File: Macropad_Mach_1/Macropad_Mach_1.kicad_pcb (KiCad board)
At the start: 2 copper layers, 88.4 x 102.5 mm, 39 parts, among them J1 Conn_01x12, J2 Conn_01x12, SW1 RotaryEncoder_Switch_MP

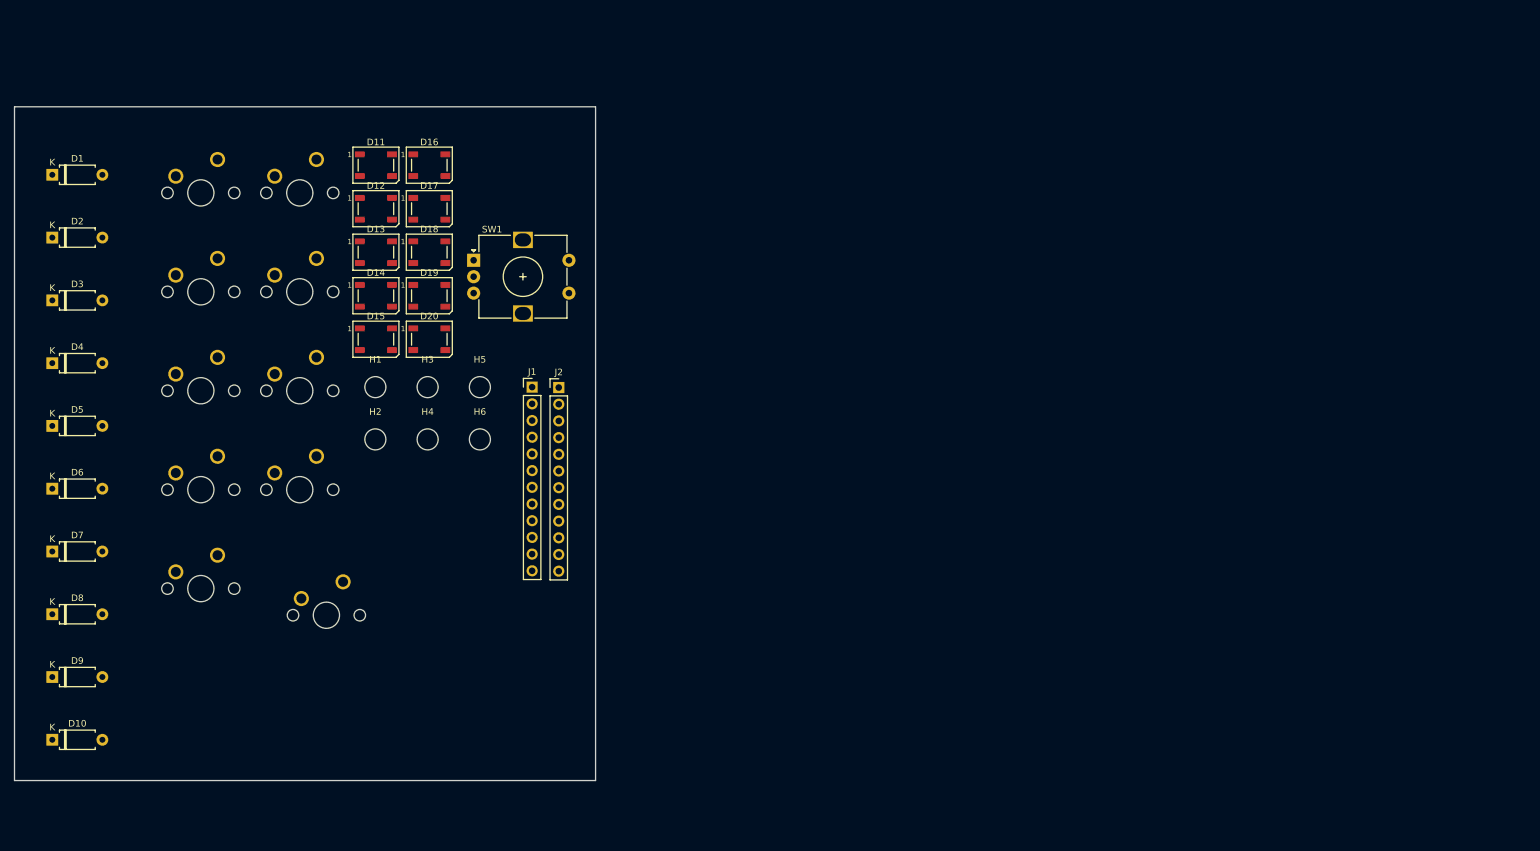
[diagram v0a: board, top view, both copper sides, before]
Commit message: feat: update PCB with APA102-2020 LEDs, keyboard layout, and encoder
- Replaced LEDs with APA102-2020
- Created the keyboard layout
- Added Edgecuts
- Routed the keys
- Integrated the encoder into the layout
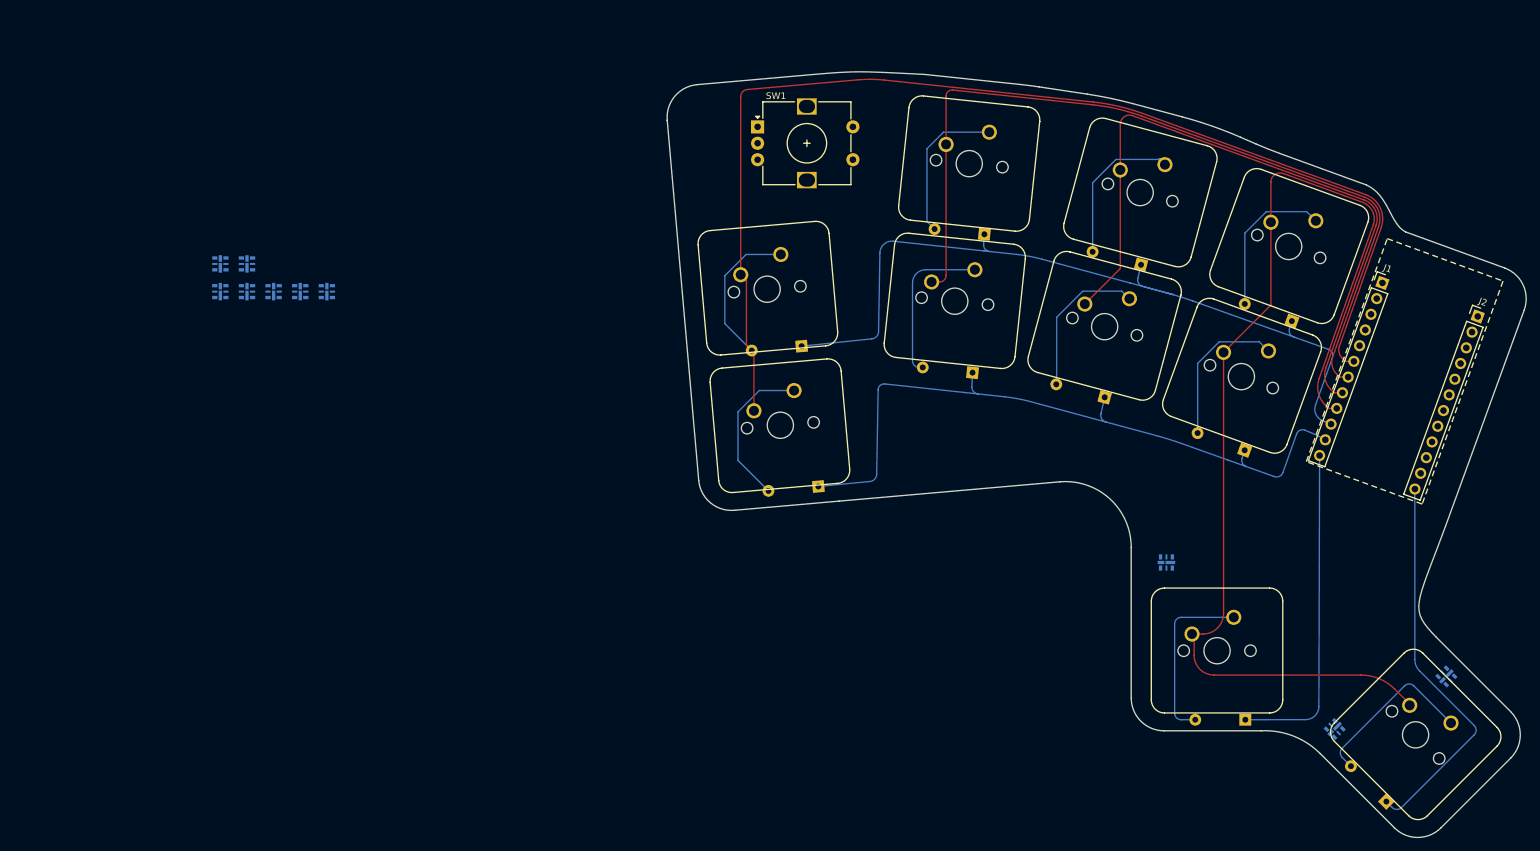
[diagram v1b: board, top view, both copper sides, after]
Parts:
- removed D11, D12, D13, D14, D15, D16, D17, D18, D19, D20: WS2812B, LED_SMD:LED_WS2812B_PLCC4_5.0x5.0mm_P3.2mm
- removed H1, H2, H3, H4, H5, H6: MountingHole, MountingHole:MountingHole_3.2mm_M3
- added D21: APA102-2020, LED_SMD:LED-APA102-2020, B.Cu at (267.6, 133.4)
- added D22: APA102-2020, LED_SMD:LED-APA102-2020, B.Cu at (250.6, 141.4)
- added D23: APA102-2020, LED_SMD:LED-APA102-2020, B.Cu at (225.0, 116.1)
- added D24: APA102-2020, LED_SMD:LED-APA102-2020, B.Cu at (85.1, 70.7)
- added D25: APA102-2020, LED_SMD:LED-APA102-2020, B.Cu at (81.1, 70.7)
- added D26: APA102-2020, LED_SMD:LED-APA102-2020, B.Cu at (97.3, 74.9)
- added D27: APA102-2020, LED_SMD:LED-APA102-2020, B.Cu at (93.2, 74.9)
- added D28: APA102-2020, LED_SMD:LED-APA102-2020, B.Cu at (89.2, 74.9)
- added D29: APA102-2020, LED_SMD:LED-APA102-2020, B.Cu at (85.1, 74.9)
- added D30: APA102-2020, LED_SMD:LED-APA102-2020, B.Cu at (81.1, 74.9)
- D1, D10, D2, D3, D4, D5, D6, D7, D8, D9: moved to B.Cu
- moved D10 203.2 mm to (258.4, 152.4), turned to 135 degrees
- moved D4 188.7 mm to (244.1, 79.4), turned to 160 degrees
- moved D8 183.1 mm to (236.9, 99.0), turned to 160 degrees
- moved D9 181.6 mm to (237.0, 140.0), turned to 180 degrees
- moved MX4 169.6 mm to (243.6, 68.0), turned to -20 degrees
- moved MX10 166.7 mm to (262.9, 142.3), turned to -45 degrees
- moved D3 165.7 mm to (221.1, 70.8), turned to 165 degrees
- moved D7 161.8 mm to (215.6, 91.0), turned to 165 degrees
- moved MX3 146.0 mm to (221.0, 59.8), turned to -15 degrees
- moved MX8 143.3 mm to (236.4, 87.8), turned to -20 degrees
- moved D2 141.8 mm to (197.3, 66.2), turned to 174 degrees
- moved MX9 141.7 mm to (232.7, 129.5)
- moved D6 141.1 mm to (195.5, 87.2), turned to 174 degrees
- moved J2 140.2 mm to (272.4, 78.6), turned to -20 degrees
- moved J1 130.3 mm to (257.9, 73.5), turned to -20 degrees
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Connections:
- J1 pad 10: Row_0 -> Col_3
- J1 pad 11: Row_1 -> Row_0
- J1 pad 12: Row_2 -> Row_1
- J1 pad 5: unconnected-(J1-Pin_5-Pad5) -> SDA
- J1 pad 6: Col_0 -> SCL
- J1 pad 7: Col_1 -> Col_0
- J1 pad 8: Col_2 -> Col_1
- J1 pad 9: Col_3 -> Col_2
- J2 pad 11: unconnected-(J2-Pin_11-Pad11) -> Row_3
- J2 pad 12: Row_3 -> Row_2
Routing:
- net Col_0: track 0.00 -> 176.0 mm
- net Col_3: track 0.00 -> 165.1 mm
- net Col_1: track 0.00 -> 127.8 mm
- net Row_0: track 0.00 -> 124.3 mm
- net Row_1: track 0.00 -> 108.4 mm
- net Col_2: track 0.00 -> 102.7 mm
- net Row_3: track 0.00 -> 59.6 mm
- net Row_2: track 0.00 -> 50.4 mm
- net Net-(D9-A): track 0.00 -> 26.8 mm
- net Net-(D10-A): track 0.00 -> 26.3 mm
- net Net-(D6-A): track 0.00 -> 24.5 mm
- net Net-(D5-A): track 0.00 -> 23.8 mm
- net Net-(D4-A): track 0.00 -> 23.5 mm
- net Net-(D7-A): track 0.00 -> 23.4 mm
- net Net-(D8-A): track 0.00 -> 23.3 mm
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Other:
- board size 88.4 x 102.5 mm -> 130.7 x 116.5 mm

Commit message: Finalized PCB routing, connected decoder, and improved design for manufacturing
- Completed trace routing for the keys
- Connected the decoder to the circuit
- Refined silkscreen for better readability
- Adjusted trace widths to meet design requirements
- Optimized clearance settings for JLCPCB manufacturing
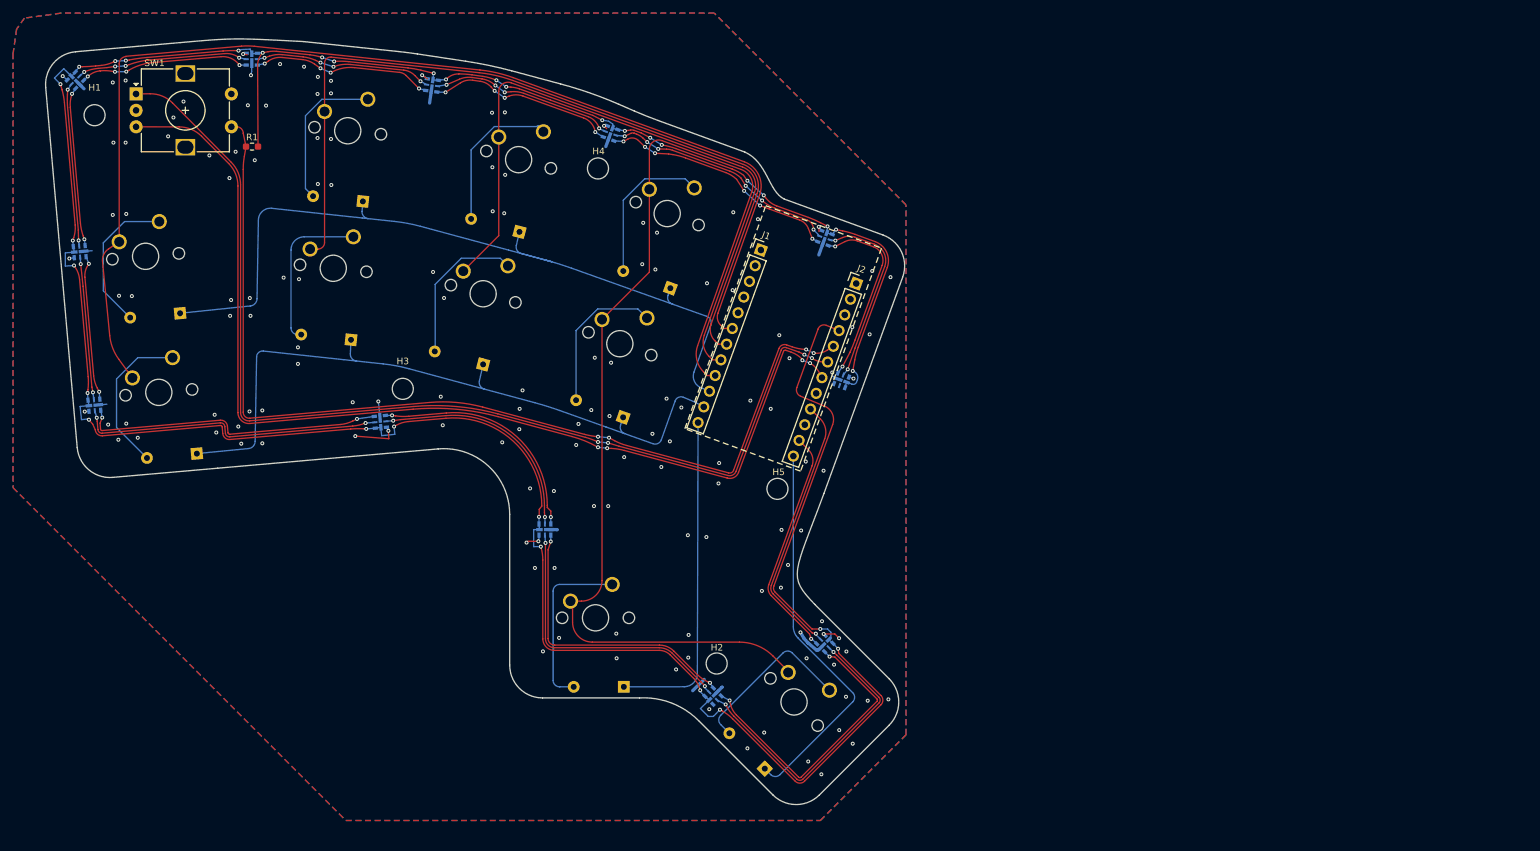
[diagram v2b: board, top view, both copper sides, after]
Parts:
- added D11: APA102-2020, LED_SMD:LED-APA102-2020, B.Cu at (173.0, 66.7)
- added D12: APA102-2020, LED_SMD:LED-APA102-2020, B.Cu at (175.6, 88.4)
- added H1: MountingHole, MountingHole:MountingHole_3.2mm_M3, F.Cu at (61.9, 48.0)
- added H2: MountingHole, MountingHole:MountingHole_3.2mm_M3, F.Cu at (156.6, 131.4)
- added H3: MountingHole, MountingHole:MountingHole_3.2mm_M3, F.Cu at (108.8, 89.7)
- added H4: MountingHole, MountingHole:MountingHole_3.2mm_M3, F.Cu at (138.5, 56.1)
- added H5: MountingHole, MountingHole:MountingHole_3.2mm_M3, F.Cu at (165.8, 104.9)
- added R1: 10K, Resistor_SMD:R_0603_1608Metric_Pad0.98x0.95mm_HandSolder, F.Cu at (85.9, 52.8)
- moved D21 94.7 mm to (173.0, 128.4), turned to 135 degrees
- moved D2 94.7 mm to (102.7, 61.1)
- moved D3 94.7 mm to (126.6, 65.8)
- moved MX6 94.7 mm to (98.2, 71.3)
- moved SW1 94.7 mm to (68.2, 44.8)
- moved D10 94.7 mm to (163.9, 147.4)
- moved D22 94.7 mm to (156.0, 136.4)
- moved D23 94.7 mm to (130.4, 111.1)
- moved D4 94.7 mm to (149.5, 74.3)
- moved D5 94.7 mm to (77.5, 99.5)
- moved D6 94.7 mm to (100.9, 82.2)
- moved D7 94.7 mm to (121.0, 85.9)
- moved D8 94.7 mm to (142.3, 94.0)
- moved D9 94.7 mm to (142.4, 135.0)
- moved J1 94.7 mm to (163.3, 68.5)
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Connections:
- D21 pad 4: SDA -> MOSI
- D21 pad 5: SCL -> SCLK
- D30 pad 2: unconnected-(D30-CKO-Pad2) -> Net-(D11-CKI)
- D30 pad 3: unconnected-(D30-SDO-Pad3) -> Net-(D11-SDI)
- J1 pad 10: Col_3 -> Row_0
- J1 pad 11: Row_0 -> Row_1
- J1 pad 12: Row_1 -> Row_2
- J1 pad 5: SDA -> unconnected-(J1-Pin_5-Pad5)
- J1 pad 6: SCL -> Col_0
- J1 pad 7: Col_0 -> Col_1
- J1 pad 8: Col_1 -> Col_2
- J1 pad 9: Col_2 -> Col_3
- J2 pad 11: Row_3 -> MOSI
- J2 pad 12: Row_2 -> Row_3
- J2 pad 8: LED_Data -> unconnected-(J2-Pin_8-Pad8)
- J2 pad 9: unconnected-(J2-Pin_9-Pad9) -> SCLK
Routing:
- net 5V: track 0.00 -> 482.9 mm, vias 0 -> 33
- net Encoder_A: track 0.00 -> 162.2 mm, vias 0 -> 4
- net Encoder_B: track 0.00 -> 160.6 mm, vias 0 -> 4
- net Encoder_Switch: track 0.00 -> 150.4 mm, vias 0 -> 4
- net Net-(D24-CKO): track 0.00 -> 47.0 mm, vias 0 -> 2
- net GND: track 0.00 -> 46.8 mm, vias 0 -> 145
- net Net-(D24-SDO): track 0.00 -> 46.5 mm, vias 0 -> 2
- net Net-(D21-CKO): track 0.00 -> 46.3 mm, vias 0 -> 2
- net Net-(D21-SDO): track 0.00 -> 45.3 mm, vias 0 -> 2
- net Net-(D22-CKO): track 0.00 -> 44.2 mm, vias 0 -> 2
- net Net-(D22-SDO): track 0.00 -> 44.0 mm, vias 0 -> 2
- net SCLK: track 0.00 -> 40.9 mm, vias 0 -> 1
- net Net-(D11-SDI): track 0.00 -> 36.6 mm, vias 0 -> 6
- net Net-(D11-CKI): track 0.00 -> 36.2 mm, vias 0 -> 6
- net MOSI: track 0.00 -> 36.0 mm, vias 0 -> 1
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- added copper zone on B.Cu, net GND
- added copper zone on F.Cu, net GND

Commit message: Feat: added Logoand Description
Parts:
- added C1: 4.7 µF, Capacitor_SMD:C_0201_0603Metric_Pad0.64x0.40mm_HandSolder, F.Cu at (171.1, 81.6)
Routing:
- net GND: track 46.8 -> 47.4 mm
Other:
- board text added: "Git: Kideya/Keybin-ItReal Macro-Pad Made by Kideya Date: 02.2025 | Rev.1"
